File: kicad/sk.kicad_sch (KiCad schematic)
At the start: 9 parts, among them J1 AC, J2 Barrel_Jack, J3 Barrel_Jack, J4 Barrel_Jack, J5 Barrel_Jack, J6 Barrel_Jack, J7 Barrel_Jack, J8 Barrel_Jack, J9 Barrel_Jack

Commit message: Post zip cleanups
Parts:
- removed J1: AC, symbol Connector:Conn_01x02_Male
- removed J8, J9: Barrel_Jack, symbol Connector:Barrel_Jack
- added J1: AC, conn-5430373:5430373, symbol Connector:Conn_01x03_Pin
- J2, J3, J4, J5, J6, J7: footprint (none) -> barrel-jack:PJ002A
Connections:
- net 230VAC/+230VAC: now also J1.1 (Pin_1)
- net 230VAC/NEUTRAL: now also J1.2 (Pin_2), J1.3 (Pin_3)
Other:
- removed sheet 9VDC7
- removed sheet 9VDC8
- removed sheet IND7
- removed sheet IND8

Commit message: Initial PCB layout
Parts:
- added H1, H2, H3, H4, H5, H6: MountingHole_Pad, MountingHole:MountingHole_2.2mm_M2_ISO14580_Pad, symbol Mechanical:MountingHole_Pad
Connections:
- net 230VAC/NEUTRAL: no longer J1.3 (Pin_3)
- net GND: now also H1.1, H2.1, H3.1, H4.1, H5.1, H6.1

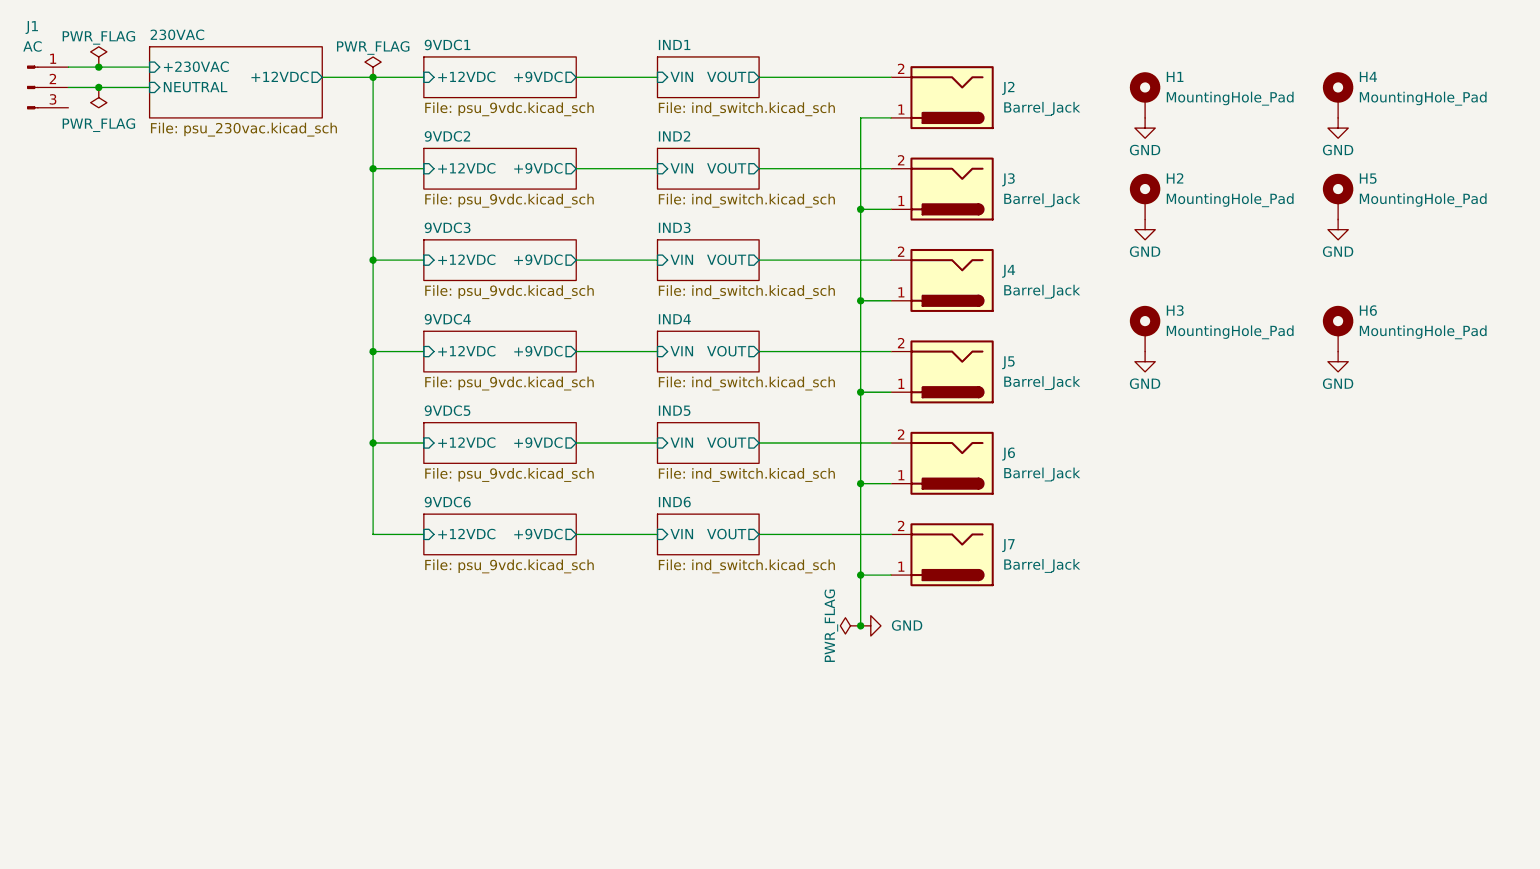
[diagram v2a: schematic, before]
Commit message: Make PCB rework
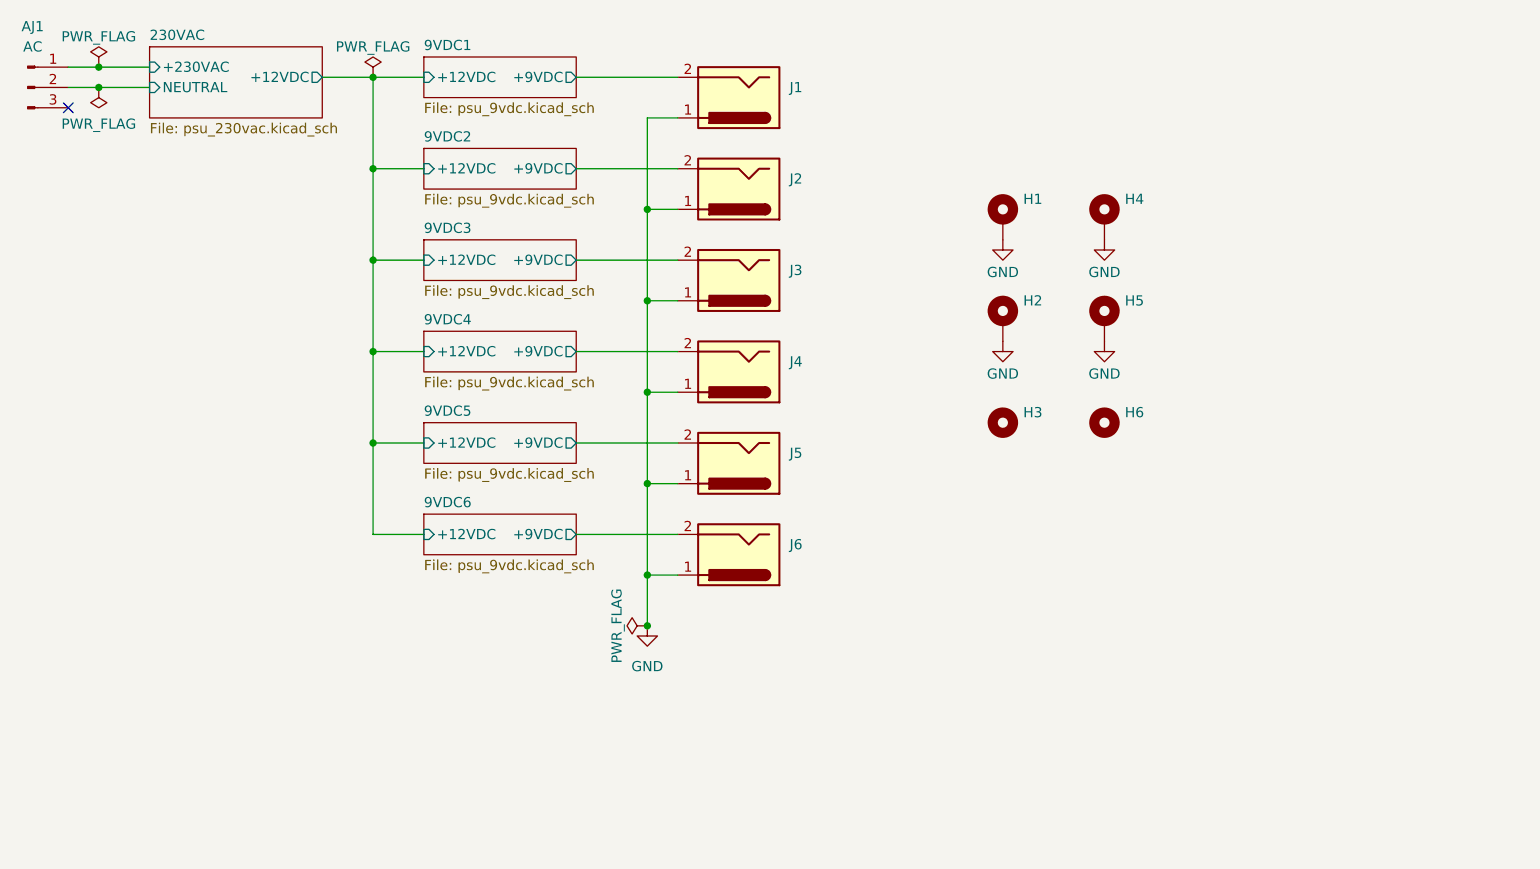
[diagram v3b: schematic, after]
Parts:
- removed H3, H6: MountingHole_Pad, MountingHole:MountingHole_2.2mm_M2_ISO14580_Pad, symbol Mechanical:MountingHole_Pad
- added H3, H6: MountingHole, MountingHole:MountingHole_2mm, symbol Mechanical:MountingHole
- renumbered J1 to AJ1, J2 to J1, J3 to J2, J4 to J3, J5 to J4, J6 to J5, J7 to J6
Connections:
- net IND1/VOUT is gone; now on net 9VDC1/+9VDC: J1.2
- net IND2/VOUT is gone; now on net 9VDC2/+9VDC: J2.2
- net IND3/VOUT is gone; now on net 9VDC3/+9VDC: J3.2
- net IND4/VOUT is gone; now on net 9VDC4/+9VDC: J4.2
- net IND5/VOUT is gone; now on net 9VDC5/+9VDC: J5.2
- net IND6/VOUT is gone; now on net 9VDC6/+9VDC: J6.2
- no-connect marks 0 -> 1
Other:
- removed sheet IND1
- removed sheet IND2
- removed sheet IND3
- removed sheet IND4
- removed sheet IND5
- removed sheet IND6
- moved on the sheet: H1, H2, H4, H5, J1, J2, J3, J4, J5, J6
